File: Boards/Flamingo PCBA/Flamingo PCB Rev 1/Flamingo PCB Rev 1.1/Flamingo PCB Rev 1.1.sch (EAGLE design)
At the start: 11 parts

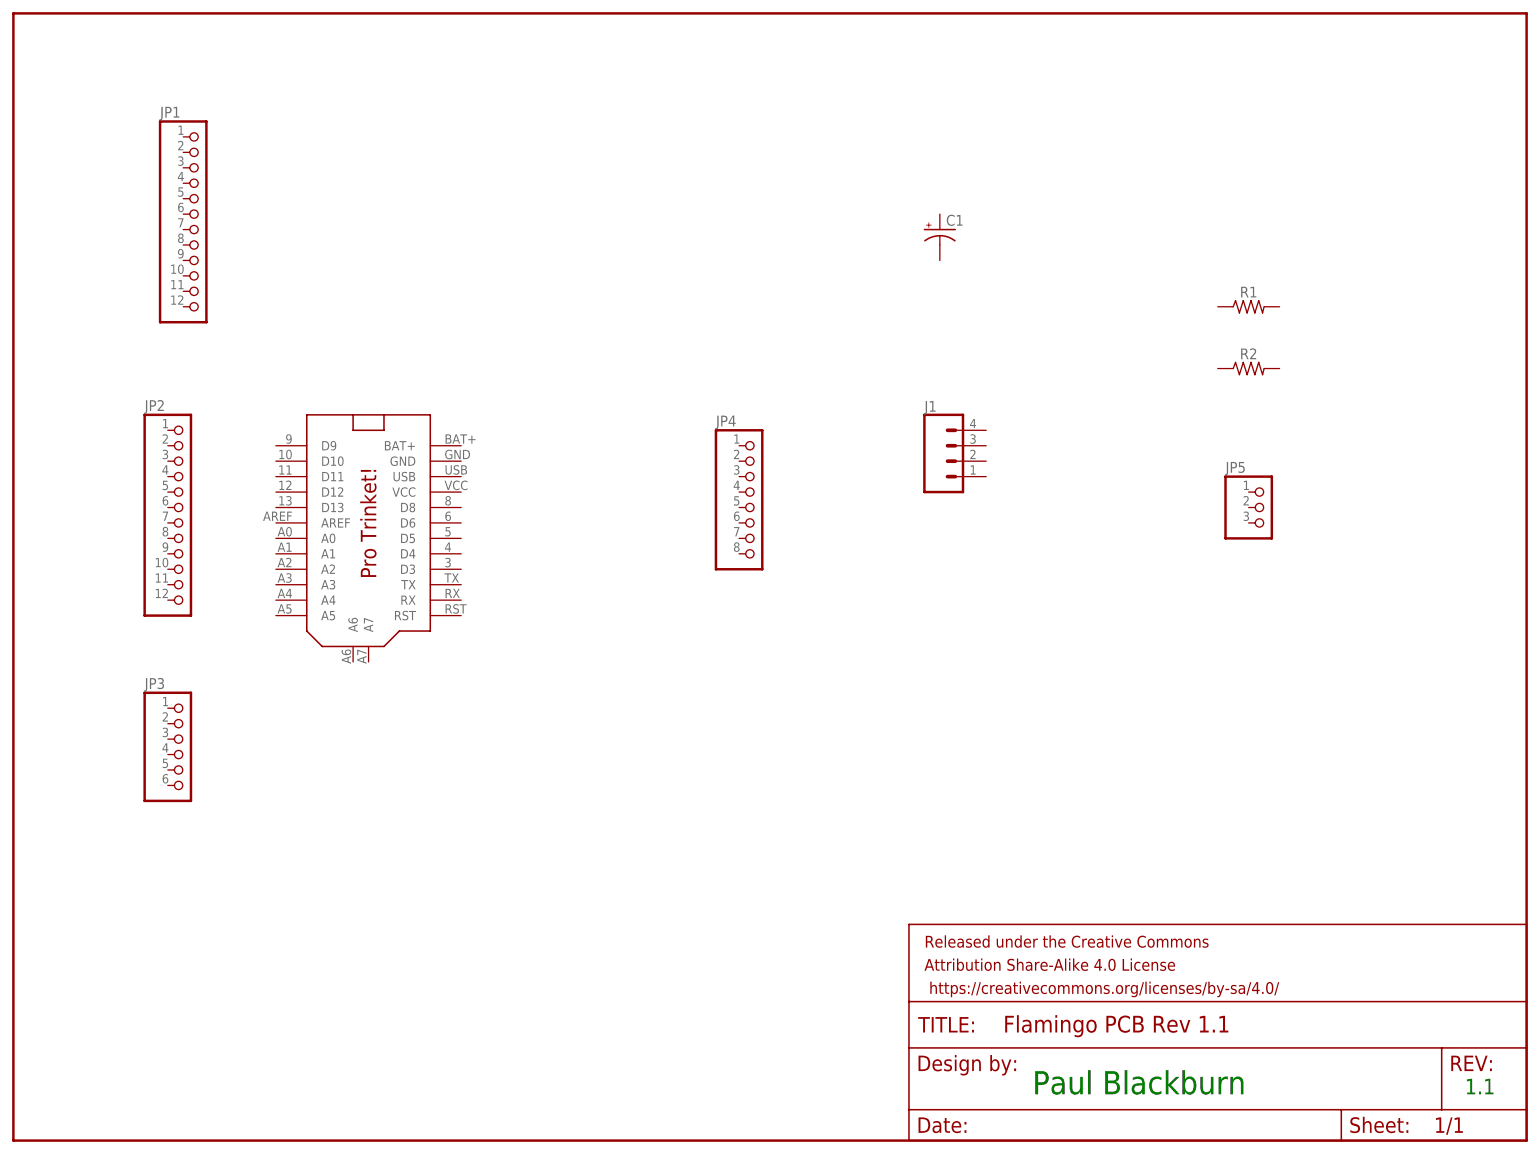
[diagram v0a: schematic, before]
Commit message: Completed preliminary component layout
Decided to just glue the 5 wires from the remote and 4 for the lights
to the underside of the PCB.
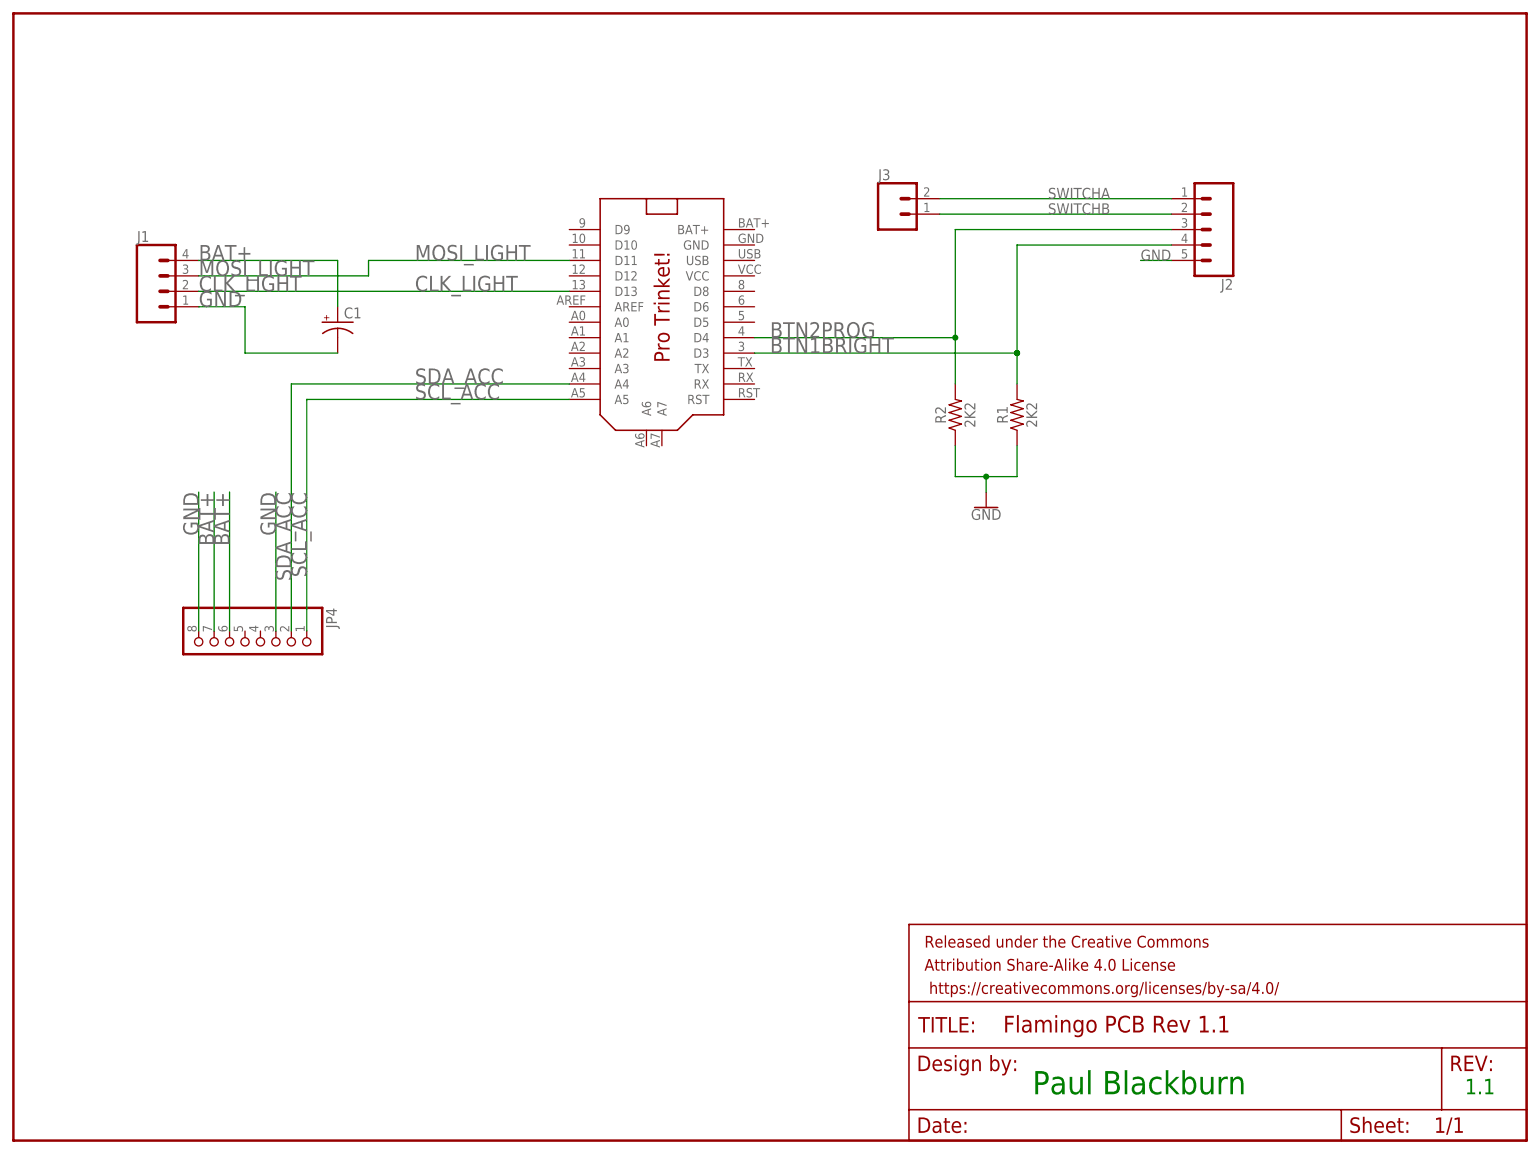
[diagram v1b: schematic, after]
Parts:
- removed JP1, JP2: (no value), adafruit:PINHD-1X12-CB
- removed JP3: (no value), adafruit:PINHD-1X6CB
- removed JP5: (no value), adafruit:PINHD-1X3CB
- added J2: (no value), SparkFun-Connectors:CONN_05
- added J3: (no value), SparkFun-Connectors:CONN_02
- R1, R2: value (none) -> 2K2
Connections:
- new net BAT+: C1.+, J1.4, JP4.6, JP4.7
- new net BTN1BRIGHT: J2.4, R1.2, U$1.D3
- new net BTN2PROG: J2.3, R2.2, U$1.D4
- new net CLK_LIGHT: J1.2, U$1.D13
- new net GND: C1.-, J1.1, J2.5, JP4.3, JP4.8, R1.1, R2.1
- new net MOSI_LIGHT: J1.3, U$1.D11
- new net SCL_ACC: JP4.1, U$1.A5
- new net SDA_ACC: JP4.2, U$1.A4
- new net SWITCHA: J2.1, J3.2
- new net SWITCHB: J2.2, J3.1
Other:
- moved on the sheet: C1, J1, JP4, R1, R2
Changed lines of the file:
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@@
 <parts>
 <part name="FRAME1" library="SparkFun-Aesthetics" library_urn="urn:adsk.eagle:library:507" deviceset="FRAME-LETTER" device=""/>
-<part name="JP1" library="adafruit" library_urn="urn:adsk.eagle:library:420" deviceset="PINHD-1X12" device="-CB"/>
-<part name="JP2" library="adafruit" library_urn="urn:adsk.eagle:library:420" deviceset="PINHD-1X12" device="-CB"/>
-<part name="JP3" library="adafruit" library_urn="urn:adsk.eagle:library:420" deviceset="PINHD-1X6" device="CB"/>
 <part name="C1" library="adafruit" library_urn="urn:adsk.eagle:library:420" deviceset="CPOL-US" device="E5-6"/>
+<part name="JP4" library="adafruit" library_urn="urn:adsk.eagle:library:420" deviceset="PINHD-1X8" device="CLEANBIG"/>
+<part name="R1" library="SparkFun-Resistors" library_urn="urn:adsk.eagle:library:532" deviceset="RESISTOR" device="AXIAL-0.3" value="2K2"/>
+<part name="R2" library="SparkFun-Resistors" library_urn="urn:adsk.eagle:library:532" deviceset="RESISTOR" device="AXIAL-0.3" value="2K2"/>
+<part name="J1" library="SparkFun-Connectors" library_urn="urn:adsk.eagle:library:513" deviceset="CONN_04" device=""/>
+<part name="GND1" library="SparkFun-PowerSymbols" library_urn="urn:adsk.eagle:library:530" deviceset="GND" device=""/>
 <part name="U$1" library="adafruit" library_urn="urn:adsk.eagle:library:420" deviceset="PRO_TRINKET" device=""/>
-<part name="JP4" library="adafruit" library_urn="urn:adsk.eagle:library:420" deviceset="PINHD-1X8" device="CLEANBIG"/>
-<part name="JP5" library="adafruit" library_urn="urn:adsk.eagle:library:420" deviceset="PINHD-1X3" device="CB"/>
-<part name="R1" library="SparkFun-Resistors" library_urn="urn:adsk.eagle:library:532" deviceset="RESISTOR" device="AXIAL-0.3" value=" "/>
-<part name="R2" library="SparkFun-Resistors" library_urn="urn:adsk.eagle:library:532" deviceset="RESISTOR" device="AXIAL-0.3" value=" "/>
-<part name="J1" library="SparkFun-Connectors" library_urn="urn:adsk.eagle:library:513" deviceset="CONN_04" device=""/>
+<part name="J2" library="SparkFun-Connectors" library_urn="urn:adsk.eagle:library:513" deviceset="CONN_05" device=""/>
+<part name="J3" library="SparkFun-Connectors" library_urn="urn:adsk.eagle:library:513" deviceset="CONN_02" device=""/>
 </parts>
 <sheets>
@@
 <instance part="FRAME1" gate="G$1" x="0" y="0"/>
 <instance part="FRAME1" gate="V" x="147.32" y="0"/>
-<instance part="JP1" gate="G$1" x="30.48" y="152.4"/>
-<instance part="JP2" gate="G$1" x="27.94" y="104.14"/>
-<instance part="JP3" gate="A" x="27.94" y="63.5"/>
-<instance part="C1" gate="G$1" x="152.4" y="149.86"/>
-<instance part="U$1" gate="G$1" x="58.42" y="101.6"/>
-<instance part="JP4" gate="G$1" x="121.92" y="106.68"/>
-<instance part="JP5" gate="A" x="205.74" y="104.14"/>
-<instance part="R1" gate="G$1" x="203.2" y="137.16"/>
-<instance part="R2" gate="G$1" x="203.2" y="127"/>
-<instance part="J1" gate="G$1" x="154.94" y="111.76"/>
+<instance part="C1" gate="G$1" x="53.34" y="134.62"/>
+<instance part="JP4" gate="G$1" x="40.64" y="81.28" rot="R270"/>
+<instance part="R1" gate="G$1" x="165.1" y="119.38" rot="R90"/>
+<instance part="R2" gate="G$1" x="154.94" y="119.38" rot="R90"/>
+<instance part="J1" gate="G$1" x="25.4" y="139.7"/>
+<instance part="GND1" gate="1" x="160.02" y="104.14"/>
+<instance part="U$1" gate="G$1" x="106.68" y="137.16"/>
+<instance part="J2" gate="G$1" x="198.12" y="149.86" rot="R180"/>
+<instance part="J3" gate="G$1" x="144.78" y="152.4"/>
 </instances>
 <busses>
 </busses>
 <nets>
+<net name="BAT+" class="0">
+<segment>
+<pinref part="JP4" gate="G$1" pin="7"/>
+<wire x1="33.02" y1="83.82" x2="33.02" y2="106.68" width="0.1524" layer="91"/>
+<label x="30.48" y="106.68" size="2.54" layer="95" font="vector" rot="R270"/>
+</segment>
+<segment>
+<pinref part="JP4" gate="G$1" pin="6"/>
+<wire x1="35.56" y1="83.82" x2="35.56" y2="106.68" width="0.1524" layer="91"/>
+<label x="33.02" y="106.68" size="2.54" layer="95" font="vector" rot="R270"/>
+</segment>
+<segment>
+<pinref part="J1" gate="G$1" pin="4"/>
+<label x="30.48" y="144.78" size="2.54" layer="95" font="vector"/>
+<wire x1="30.48" y1="144.78" x2="53.34" y2="144.78" width="0.1524" layer="91"/>
+<pinref part="C1" gate="G$1" pin="+"/>
+<wire x1="53.34" y1="144.78" x2="53.34" y2="137.16" width="0.1524" layer="91"/>
+</segment>
+</net>
+<net name="GND" class="0">
+<segment>
+<pinref part="JP4" gate="G$1" pin="8"/>
+<wire x1="30.48" y1="83.82" x2="30.48" y2="106.68" width="0.1524" layer="91"/>
+<label x="27.94" y="106.68" size="2.54" layer="95" font="vector" rot="R270"/>
+</segment>
+<segment>
+<pinref part="J1" gate="G$1" pin="1"/>
+<wire x1="30.48" y1="137.16" x2="38.1" y2="137.16" width="0.1524" layer="91"/>
+<label x="30.48" y="137.16" size="2.54" layer="95" font="vector"/>
+<pinref part="C1" gate="G$1" pin="-"/>
+<wire x1="53.34" y1="129.54" x2="38.1" y2="129.54" width="0.1524" layer="91"/>
+<wire x1="38.1" y1="129.54" x2="38.1" y2="137.16" width="0.1524" layer="91"/>
+</segment>
+<segment>
+<pinref part="R1" gate="G$1" pin="1"/>
+<wire x1="165.1" y1="114.3" x2="165.1" y2="109.22" width="0.1524" layer="91"/>
+<wire x1="165.1" y1="109.22" x2="160.02" y2="109.22" width="0.1524" layer="91"/>
+<pinref part="GND1" gate="1" pin="GND"/>
+<wire x1="160.02" y1="109.22" x2="160.02" y2="106.68" width="0.1524" layer="91"/>
+<pinref part="R2" gate="G$1" pin="1"/>
+<wire x1="154.94" y1="114.3" x2="154.94" y2="109.22" width="0.1524" layer="91"/>
+<wire x1="160.02" y1="109.22" x2="154.94" y2="109.22" width="0.1524" layer="91"/>
+<junction x="160.02" y="109.22"/>
+</segment>
+<segment>
+<pinref part="JP4" gate="G$1" pin="3"/>
+<wire x1="43.18" y1="83.82" x2="43.18" y2="106.68" width="0.1524" layer="91"/>
+<label x="40.64" y="106.68" size="2.54" layer="95" font="vector" rot="R270"/>
+</segment>
+<segment>
+<pinref part="J2" gate="G$1" pin="5"/>
+<wire x1="190.5" y1="144.78" x2="185.42" y2="144.78" width="0.1524" layer="91"/>
+<label x="185.42" y="144.78" size="1.778" layer="95"/>
+</segment>
+</net>
+<net name="BTN2PROG" class="0">
+<segment>
+<pinref part="R2" gate="G$1" pin="2"/>
+<wire x1="154.94" y1="132.08" x2="154.94" y2="124.46" width="0.1524" layer="91"/>
+<label x="124.46" y="132.08" size="2.54" layer="95" font="vector"/>
+<junction x="154.94" y="132.08"/>
+<wire x1="154.94" y1="132.08" x2="121.92" y2="132.08" width="0.1524" layer="91"/>
+<pinref part="U$1" gate="G$1" pin="D4"/>
+<pinref part="J2" gate="G$1" pin="3"/>
+<wire x1="154.94" y1="149.86" x2="190.5" y2="149.86" width="0.1524" layer="91"/>
+<wire x1="154.94" y1="132.08" x2="154.94" y2="149.86" width="0.1524" layer="91"/>
+</segment>
+</net>
+<net name="BTN1BRIGHT" class="0">
+<segment>
+<pinref part="R1" gate="G$1" pin="2"/>
+<wire x1="165.1" y1="129.54" x2="165.1" y2="124.46" width="0.1524" layer="91"/>
+<label x="124.46" y="129.54" size="2.54" layer="95" font="vector"/>
+<wire x1="165.1" y1="129.54" x2="121.92" y2="129.54" width="0.1524" layer="91"/>
+<junction x="165.1" y="129.54"/>
+<pinref part="U$1" gate="G$1" pin="D3"/>
+<wire x1="165.1" y1="129.54" x2="165.1" y2="147.32" width="0.1524" layer="91"/>
+<junction x="165.1" y="129.54"/>
+<pinref part="J2" gate="G$1" pin="4"/>
+<wire x1="165.1" y1="147.32" x2="190.5" y2="147.32" width="0.1524" layer="91"/>
+</segment>
+</net>
+<net name="CLK_LIGHT" class="0">
+<segment>
+<pinref part="J1" gate="G$1" pin="2"/>
+<label x="30.48" y="139.7" size="2.54" layer="95" font="vector"/>
+<label x="66.04" y="139.7" size="2.54" layer="95" font="vector"/>
+<wire x1="30.48" y1="139.7" x2="91.44" y2="139.7" width="0.1524" layer="91"/>
+<pinref part="U$1" gate="G$1" pin="D13"/>
+</segment>
+</net>
+<net name="SDA_ACC" class="0">
+<segment>
+<label x="66.04" y="124.46" size="2.54" layer="95" font="vector"/>
+<pinref part="JP4" gate="G$1" pin="2"/>
+<wire x1="91.44" y1="124.46" x2="45.72" y2="124.46" width="0.1524" layer="91"/>
+<wire x1="45.72" y1="83.82" x2="45.72" y2="124.46" width="0.1524" layer="91"/>
+<label x="43.18" y="106.68" size="2.54" layer="95" font="vector" rot="R270"/>
+<pinref part="U$1" gate="G$1" pin="A4"/>
+</segment>
+</net>
+<net name="SCL_ACC" class="0">
+<segment>
+<pinref part="JP4" gate="G$1" pin="1"/>
+<wire x1="48.26" y1="83.82" x2="48.26" y2="121.92" width="0.1524" layer="91"/>
+<label x="45.72" y="106.68" size="2.54" layer="95" font="vector" rot="R270"/>
+<label x="66.04" y="121.92" size="2.54" layer="95" font="vector"/>
+<wire x1="48.26" y1="121.92" x2="91.44" y2="121.92" width="0.1524" layer="91"/>
+<pinref part="U$1" gate="G$1" pin="A5"/>
+</segment>
+</net>
+<net name="MOSI_LIGHT" class="0">
+<segment>
+<pinref part="J1" gate="G$1" pin="3"/>
+<label x="30.48" y="142.24" size="2.54" layer="95" font="vector"/>
+<wire x1="30.48" y1="142.24" x2="58.42" y2="142.24" width="0.1524" layer="91"/>
+<wire x1="58.42" y1="142.24" x2="58.42" y2="144.78" width="0.1524" layer="91"/>
+<label x="66.04" y="144.78" size="2.54" layer="95" font="vector"/>
+<pinref part="U$1" gate="G$1" pin="D11"/>
+<wire x1="91.44" y1="144.78" x2="58.42" y2="144.78" width="0.1524" layer="91"/>
+</segment>
+</net>
+<net name="SWITCHB" class="0">
+<segment>
+<pinref part="J3" gate="G$1" pin="1"/>
+<label x="170.18" y="152.4" size="1.778" layer="95"/>
+<pinref part="J2" gate="G$1" pin="2"/>
+<wire x1="190.5" y1="152.4" x2="152.4" y2="152.4" width="0.1524" layer="91"/>
+</segment>
+</net>
+<net name="SWITCHA" class="0">
+<segment>
+<pinref part="J3" gate="G$1" pin="2"/>
+<wire x1="152.4" y1="154.94" x2="190.5" y2="154.94" width="0.1524" layer="91"/>
+<label x="170.18" y="154.94" size="1.778" layer="95"/>
+<pinref part="J2" gate="G$1" pin="1"/>
+</segment>
+</net>
 </nets>
 </sheet>
